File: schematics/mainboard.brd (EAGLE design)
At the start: 68.6 x 53.3 mm, 11 parts, among them IC2 L293D

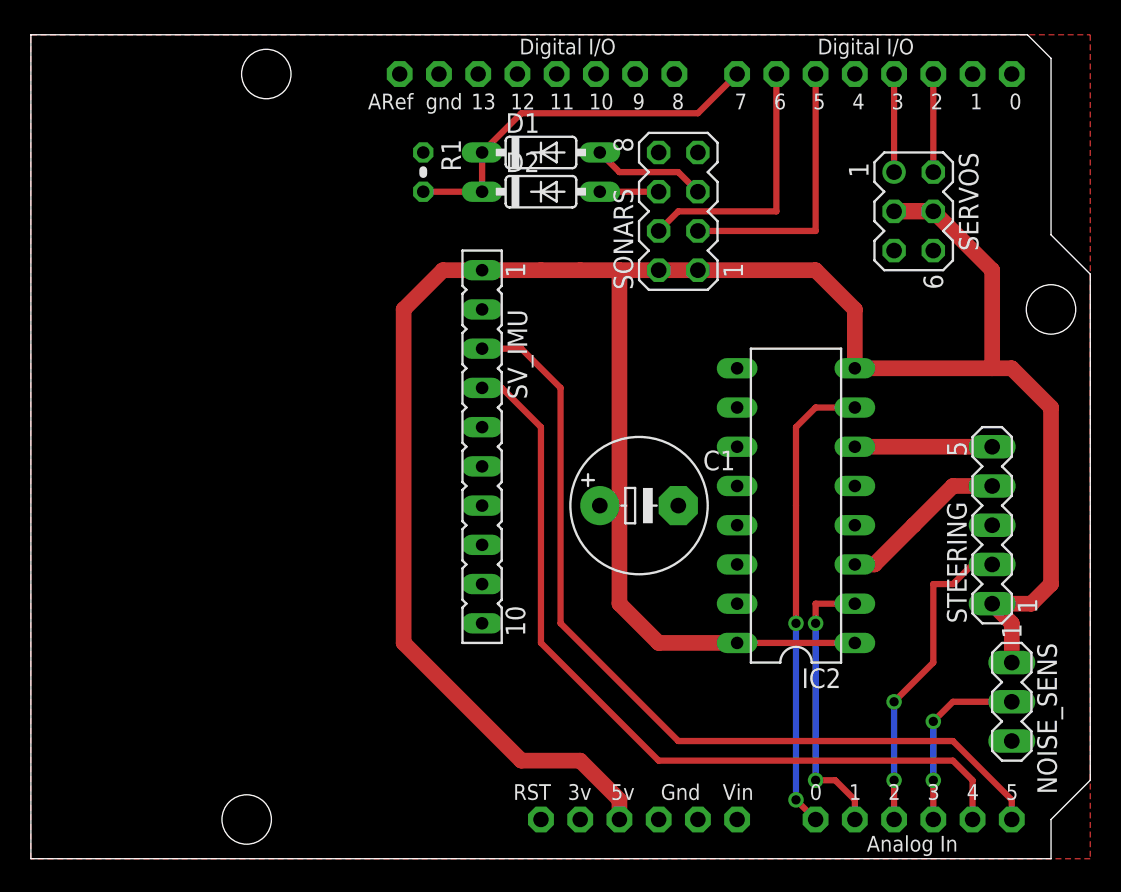
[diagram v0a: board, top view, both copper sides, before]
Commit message: Switched to proper servo. Updated PCB. Did not update for new IMU
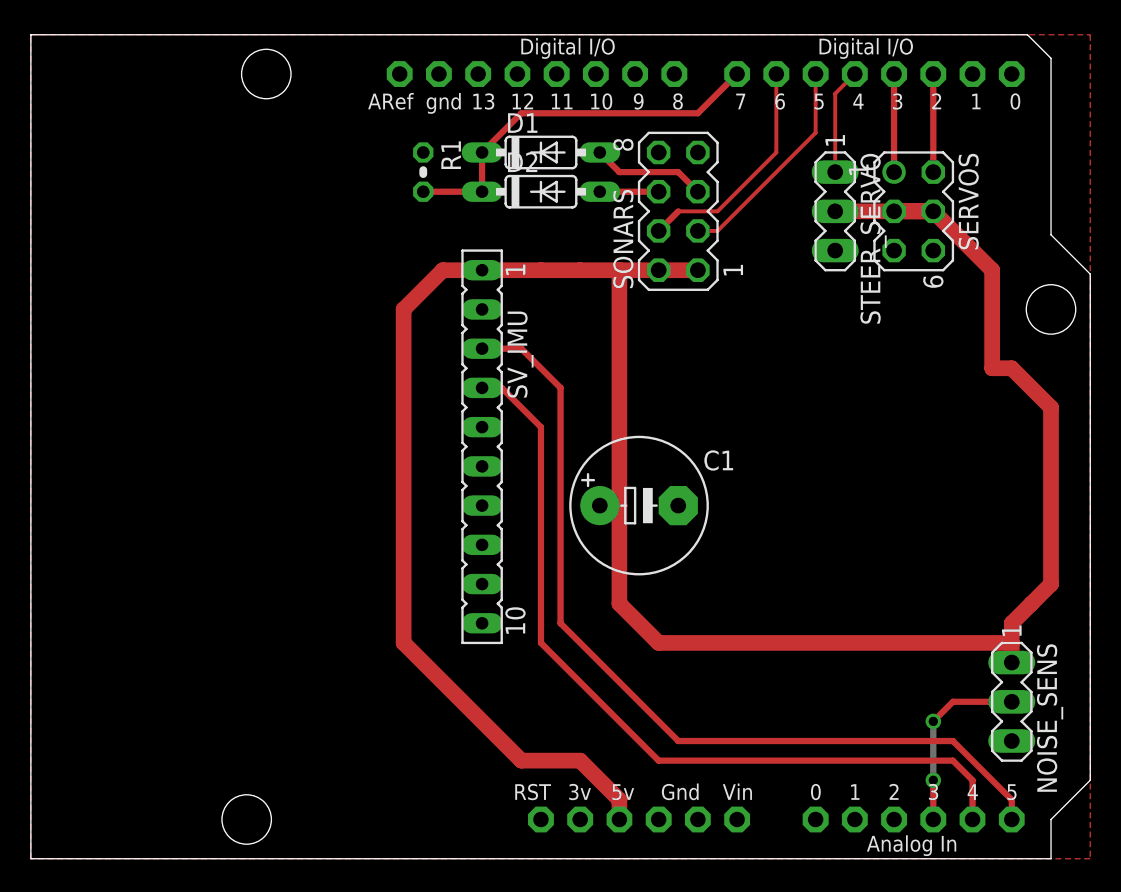
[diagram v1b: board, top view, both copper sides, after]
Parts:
- removed IC2: L293D, st-microelectronics:DIL16
- removed STEERING: (no value), con-lstb:MA05-1
- added STEER_SERVO: (no value), con-lstb:MA03-1
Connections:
- removed net N$3: IC2.3, STEERING.4
- removed net N$4: IC2.6, STEERING.5
- removed net STEER_1: IC2.2, U$1.A1
- removed net STEER_2: IC2.7, U$1.A0
- removed net STEER_POS: STEERING.2, U$1.A2
- new net STEER_SIGNAL: STEER_SERVO.1, U$1.D4
- net +5V: now also STEER_SERVO.2; no longer IC2.1, IC2.16, IC2.8, STEERING.1
- net GND: now also STEER_SERVO.3; no longer IC2.10, IC2.12, IC2.13, IC2.15, IC2.4, IC2.5, IC2.9, STEERING.3
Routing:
- net STEER_2: track 30.3 -> 0.00 mm, vias 2 -> 0
- net STEER_POS: track 20.6 -> 0.00 mm, vias 2 -> 0
- net STEER_1: track 18.3 -> 0.00 mm, vias 2 -> 0
- net +5V: track 166.0 -> 153.5 mm
- net N$3: track 11.0 -> 0.00 mm
- net N$4: track 8.89 -> 0.00 mm
- net STEER_SIGNAL: track 0.00 -> 6.88 mm
- net F_TRIG: track 17.8 -> 14.1 mm
- net B_TRIG: track 17.0 -> 14.8 mm
